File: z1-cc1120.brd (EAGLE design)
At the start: 100 x 50 mm, 12 parts, among them X1 PN61729-S

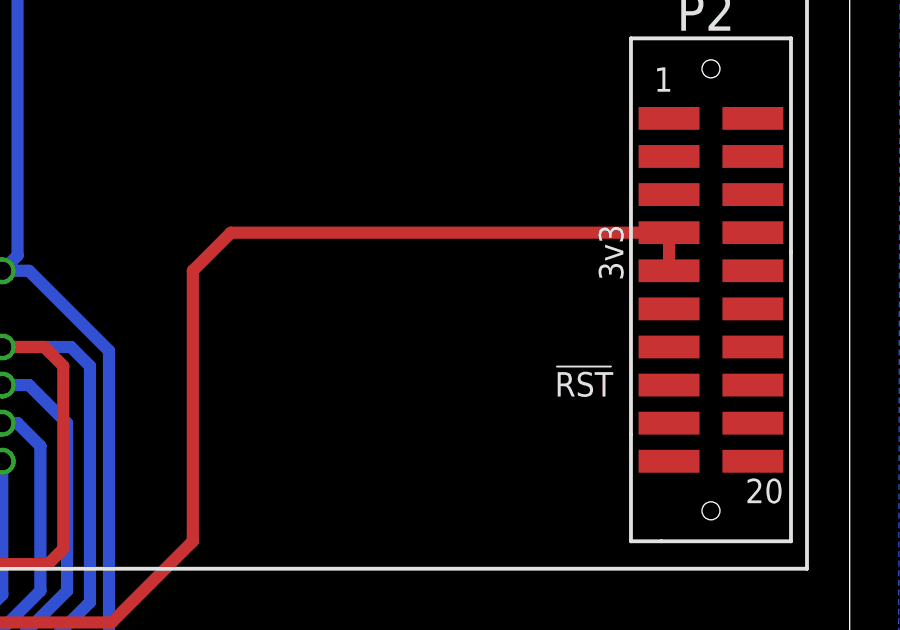
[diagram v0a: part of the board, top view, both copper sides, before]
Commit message: !RESET pullup added
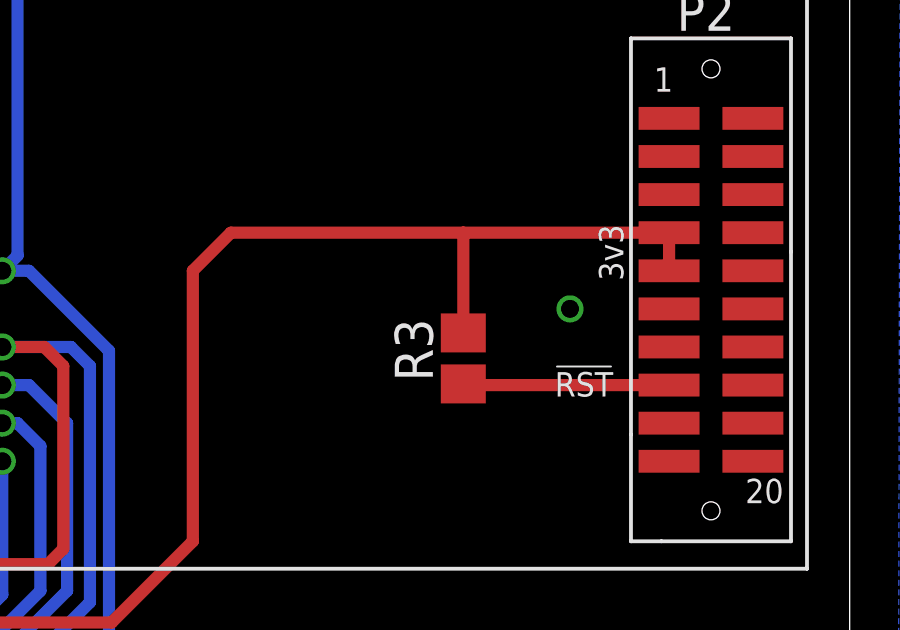
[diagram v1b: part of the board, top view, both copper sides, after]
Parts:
- added R3: 1K, resistor:R0805
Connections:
- new net N$1: R3.1, U$2.RESET
- net RADIO_3V3: now also R3.2
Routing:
- net N$1: track 0.00 -> 6.90 mm
- net RADIO_3V3: track 48.2 -> 51.5 mm
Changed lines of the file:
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@@
 <attribute name="VALUE" x="63.881" y="-0.254" size="1.27" layer="27"/>
 </element>
+<element name="R3" library="resistor" package="R0805" value="1K" x="87.122" y="20.574" rot="R90"/>
 </elements>
 <signals>
@@
 <via x="96.901" y="5.715" extent="1-16" drill="0.6" shape="octagon"/>
 <via x="59.309" y="33.02" extent="1-16" drill="0.6"/>
+<via x="90.678" y="22.225" extent="1-16" drill="0.6"/>
 </signal>
 <signal name="RADIO_3V3">
@@
 <wire x1="78.105" y1="14.478" x2="78.105" y2="23.495" width="0.4064" layer="1"/>
 <wire x1="78.105" y1="23.495" x2="79.375" y2="24.765" width="0.4064" layer="1"/>
-<wire x1="79.375" y1="24.765" x2="93.98" y2="24.765" width="0.4064" layer="1"/>
+<wire x1="79.375" y1="24.765" x2="87.122" y2="24.765" width="0.4064" layer="1"/>
+<contactref element="R3" pad="2"/>
+<wire x1="87.122" y1="24.765" x2="93.98" y2="24.765" width="0.4064" layer="1"/>
+<wire x1="87.122" y1="21.424" x2="87.122" y2="24.765" width="0.4064" layer="1"/>
+</signal>
+<signal name="N$1">
+<contactref element="U$2" pad="RESET"/>
+<contactref element="R3" pad="1"/>
+<wire x1="93.98" y1="19.685" x2="87.122" y2="19.685" width="0.4064" layer="1"/>
+<wire x1="87.122" y1="19.685" x2="87.122" y2="19.724" width="0.4064" layer="1"/>
 </signal>
 </signals>

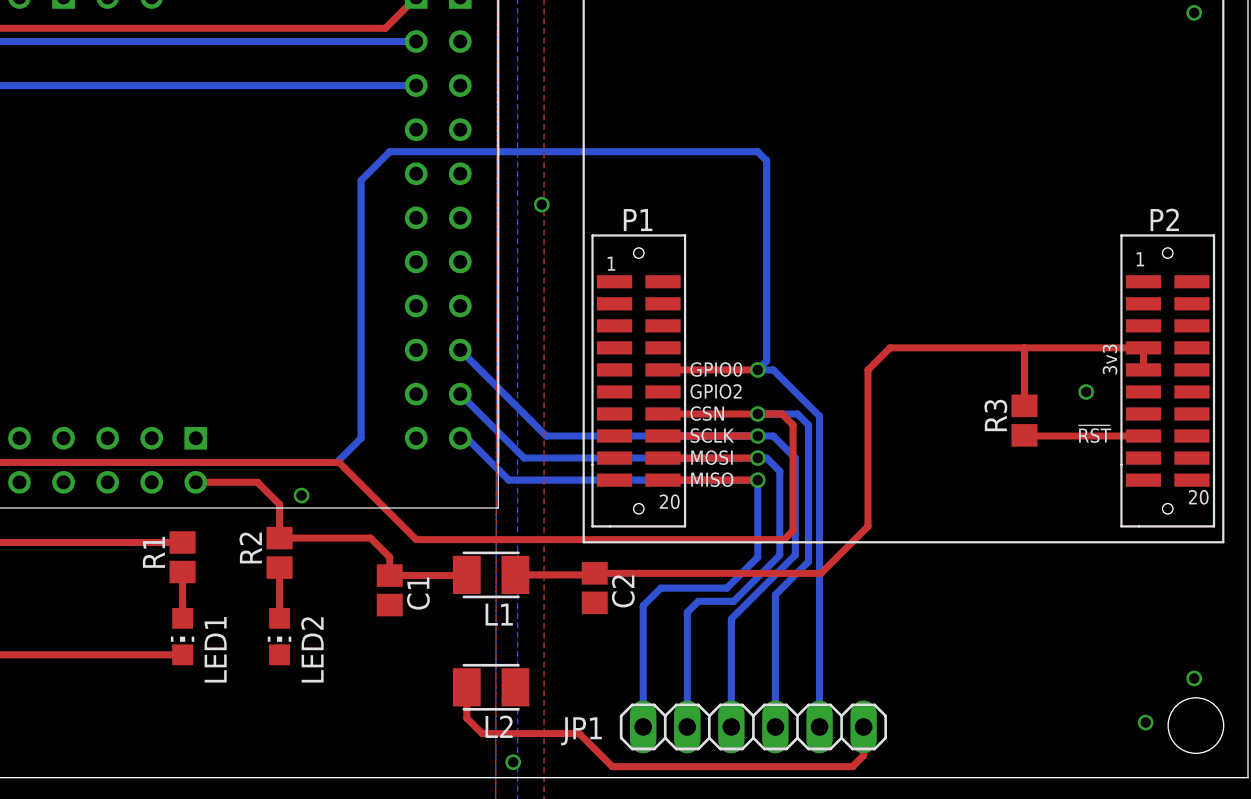
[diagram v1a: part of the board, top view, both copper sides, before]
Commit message: Added reset line from msp to cc1120
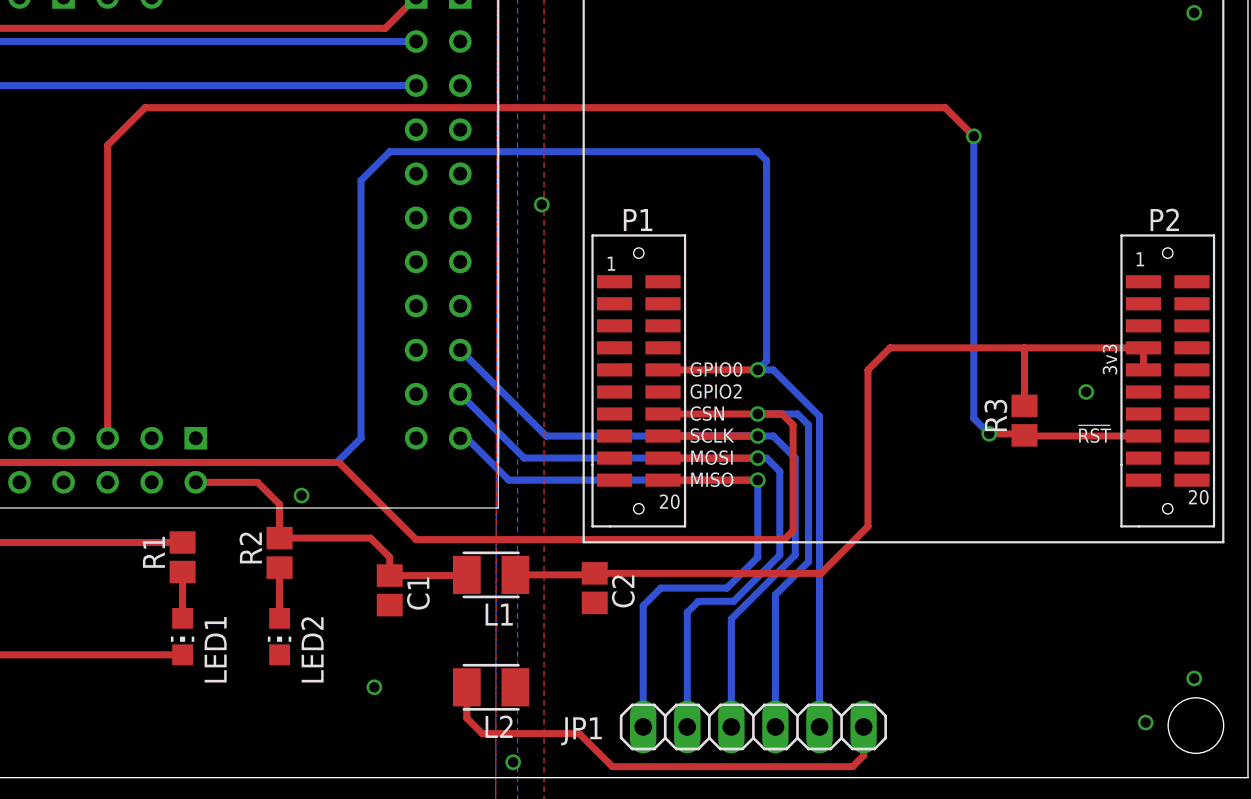
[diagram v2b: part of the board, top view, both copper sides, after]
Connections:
- removed net N$1: R3.1, U$2.RESET
- new net RADIO_!RST: R3.1, U$1.C43, U$2.RESET
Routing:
- net RADIO_!RST: track 0.00 -> 94.8 mm, vias 0 -> 2
- net N$1: track 6.90 -> 0.00 mm
- net GND: vias 1 -> 2
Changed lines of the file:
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@@
 <wire x1="77.216" y1="0.635" x2="77.851" y2="1.27" width="0.4064" layer="1"/>
 <wire x1="77.851" y1="1.27" x2="77.851" y2="2.921" width="0.4064" layer="1"/>
+<via x="49.657" y="5.207" extent="1-16" drill="0.6" shape="octagon"/>
 </signal>
 <signal name="VCC_3V3">
@@
 <wire x1="87.122" y1="21.424" x2="87.122" y2="24.765" width="0.4064" layer="1"/>
 </signal>
-<signal name="N$1">
+<signal name="RADIO_!RST">
 <contactref element="U$2" pad="RESET"/>
 <contactref element="R3" pad="1"/>
-<wire x1="93.98" y1="19.685" x2="87.122" y2="19.685" width="0.4064" layer="1"/>
-<wire x1="87.122" y1="19.685" x2="87.122" y2="19.724" width="0.4064" layer="1"/>
+<contactref element="U$1" pad="C43"/>
+<wire x1="34.29" y1="19.558" x2="34.29" y2="36.449" width="0.4064" layer="1"/>
+<wire x1="34.29" y1="36.449" x2="36.449" y2="38.608" width="0.4064" layer="1"/>
+<wire x1="36.449" y1="38.608" x2="82.55" y2="38.608" width="0.4064" layer="1"/>
+<wire x1="82.55" y1="38.608" x2="84.201" y2="36.957" width="0.4064" layer="1"/>
+<via x="84.201" y="36.957" extent="1-16" drill="0.6"/>
+<wire x1="84.201" y1="36.957" x2="84.201" y2="20.701" width="0.4064" layer="16"/>
+<wire x1="84.201" y1="20.701" x2="85.09" y2="19.812" width="0.4064" layer="16"/>
+<via x="85.09" y="19.812" extent="1-16" drill="0.6"/>
+<wire x1="85.09" y1="19.812" x2="87.034" y2="19.812" width="0.4064" layer="1"/>
+<wire x1="87.034" y1="19.812" x2="87.122" y2="19.724" width="0.4064" layer="1"/>
+<wire x1="93.98" y1="19.685" x2="87.161" y2="19.685" width="0.4064" layer="1"/>
+<wire x1="87.161" y1="19.685" x2="87.122" y2="19.724" width="0.4064" layer="1"/>
+</signal>
+<signal name="N$2">
 </signal>
 </signals>

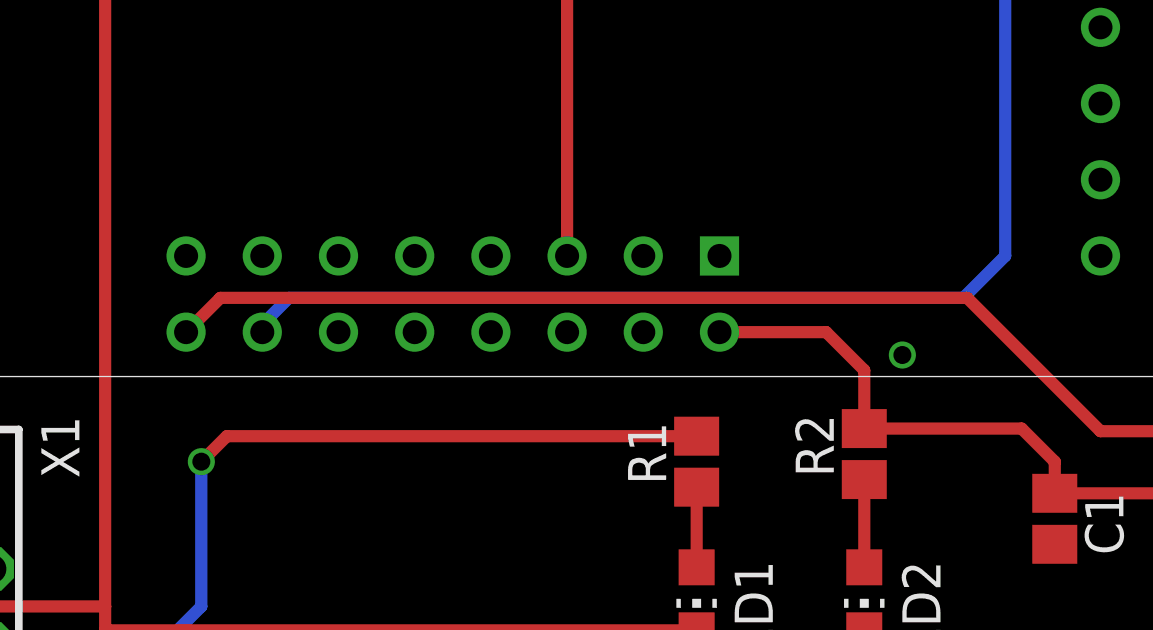
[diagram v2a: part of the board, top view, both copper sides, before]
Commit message: pins now changed to match test rig
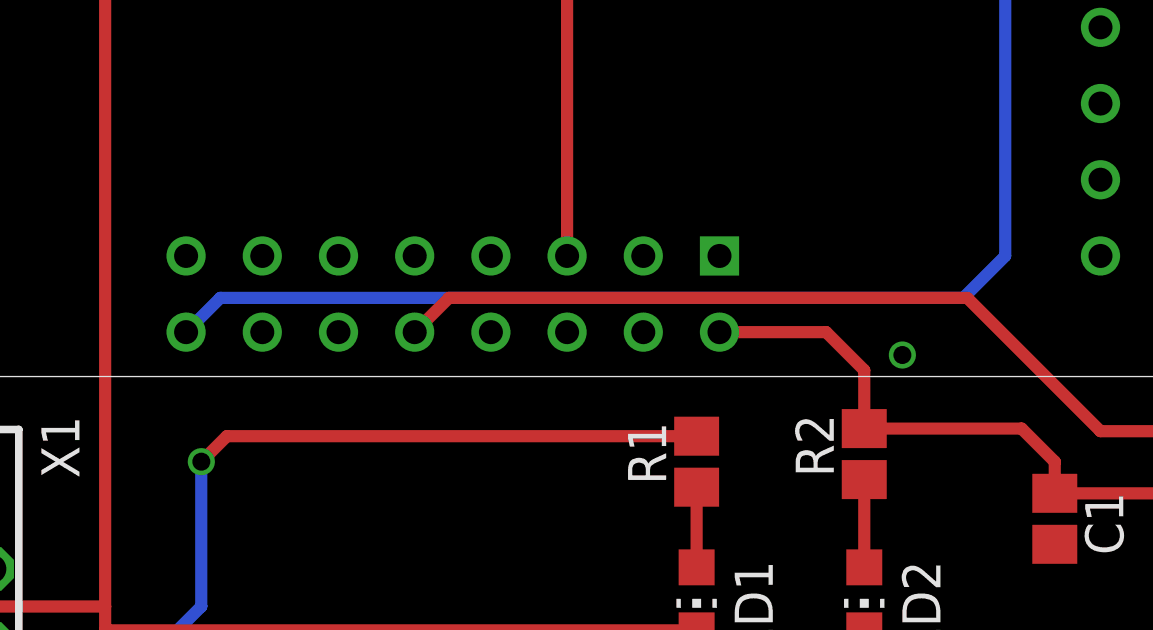
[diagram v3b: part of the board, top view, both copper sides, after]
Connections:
- net RADIO_CSN: now also U$1.C48; no longer U$1.C54
- net RADIO_INT: now also U$1.C54; no longer U$1.C52
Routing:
- net RADIO_CSN: track 89.9 -> 82.3 mm
- net RADIO_INT: track 105.4 -> 107.8 mm
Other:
- board text added: "Version 0.2"
- board text removed: "Version 0.1"
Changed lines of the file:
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@@
 <hole x="18.669" y="2.794" drill="3.2"/>
 <text x="65.405" y="9.779" size="1.778" layer="51">Z1 - CC1120 Interface</text>
-<text x="65.659" y="5.715" size="1.778" layer="51">Version 0.1</text>
+<text x="65.659" y="5.715" size="1.778" layer="51">Version 0.2</text>
 <text x="65.405" y="7.747" size="1.778" layer="51">Mountain Sensing</text>
 <text x="22.987" y="1.27" size="1.778" layer="51">PJB</text>
@@
 <signal name="RADIO_CSN">
 <contactref element="U$2" pad="CSN"/>
-<contactref element="U$1" pad="C54"/>
 <wire x1="73.787" y1="20.32" x2="73.787" y2="14.224" width="0.4064" layer="1"/>
 <wire x1="73.787" y1="14.224" x2="73.279" y2="13.716" width="0.4064" layer="1"/>
 <wire x1="73.279" y1="13.716" x2="52.07" y2="13.716" width="0.4064" layer="1"/>
 <wire x1="52.07" y1="13.716" x2="47.625" y2="18.161" width="0.4064" layer="1"/>
-<wire x1="47.625" y1="18.161" x2="22.733" y2="18.161" width="0.4064" layer="1"/>
-<wire x1="22.733" y1="18.161" x2="21.59" y2="17.018" width="0.4064" layer="1"/>
 <contactref element="JP1" pad="4"/>
 <wire x1="72.771" y1="2.921" x2="72.771" y2="10.541" width="0.4064" layer="16"/>
@@
 <wire x1="71.755" y1="20.955" x2="74.041" y2="20.955" width="0.4064" layer="16"/>
 <wire x1="66.294" y1="20.955" x2="71.755" y2="20.955" width="0.4064" layer="1"/>
+<contactref element="U$1" pad="C48"/>
+<wire x1="47.625" y1="18.161" x2="30.353" y2="18.161" width="0.4064" layer="1"/>
+<wire x1="30.353" y1="18.161" x2="29.21" y2="17.018" width="0.4064" layer="1"/>
 </signal>
 <signal name="USB_VCC">
@@
 </signal>
 <signal name="RADIO_INT">
-<contactref element="U$1" pad="C52"/>
 <contactref element="U$2" pad="GPIO0"/>
 <contactref element="JP1" pad="5"/>
-<wire x1="24.13" y1="17.018" x2="24.13" y2="17.272" width="0.4064" layer="16"/>
-<wire x1="24.13" y1="17.272" x2="25.019" y2="18.161" width="0.4064" layer="16"/>
-<wire x1="25.019" y1="18.161" x2="47.498" y2="18.161" width="0.4064" layer="16"/>
 <wire x1="47.498" y1="18.161" x2="48.895" y2="19.558" width="0.4064" layer="16"/>
 <wire x1="48.895" y1="19.558" x2="48.895" y2="34.417" width="0.4064" layer="16"/>
@@
 <wire x1="72.644" y1="23.495" x2="75.311" y2="20.828" width="0.4064" layer="16"/>
 <wire x1="75.311" y1="20.828" x2="75.311" y2="2.921" width="0.4064" layer="16"/>
+<contactref element="U$1" pad="C54"/>
+<wire x1="47.498" y1="18.161" x2="22.733" y2="18.161" width="0.4064" layer="16"/>
+<wire x1="22.733" y1="18.161" x2="21.59" y2="17.018" width="0.4064" layer="16"/>
 </signal>
 <signal name="N$24">
